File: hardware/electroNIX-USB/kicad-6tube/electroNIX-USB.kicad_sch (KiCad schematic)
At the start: 4 parts

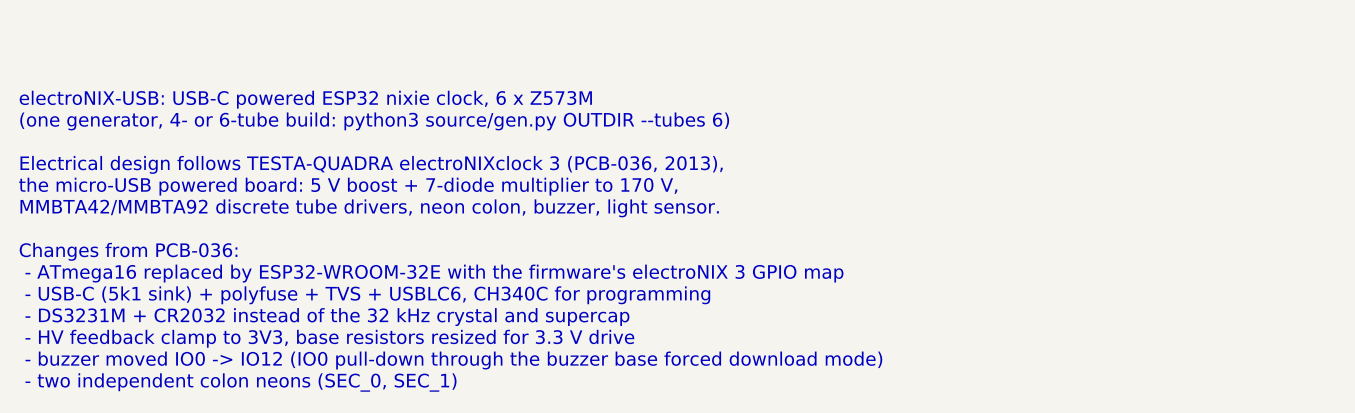
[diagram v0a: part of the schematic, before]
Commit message: electroNIX-USB: drop buzzer and DS3231, run stock firmware
Both builds now match a stock firmware profile with no changes:
BOARD_ELECTRONIX_3 for 4 tubes, BOARD_ELECTRONIX_4_6T for 6 tubes. Time
comes from NTP. IO0 gets a plain 10k pull-up. On the 4-tube build IO12
and IO15 are left open and reserved for anodes 5/6.

Co-Authored-By: Claude Opus 5.5 <noreply@anthropic.com>
Claude-Session: https://claude.ai/code/session_01AFMfevKEKDGbci8uJGhf4W
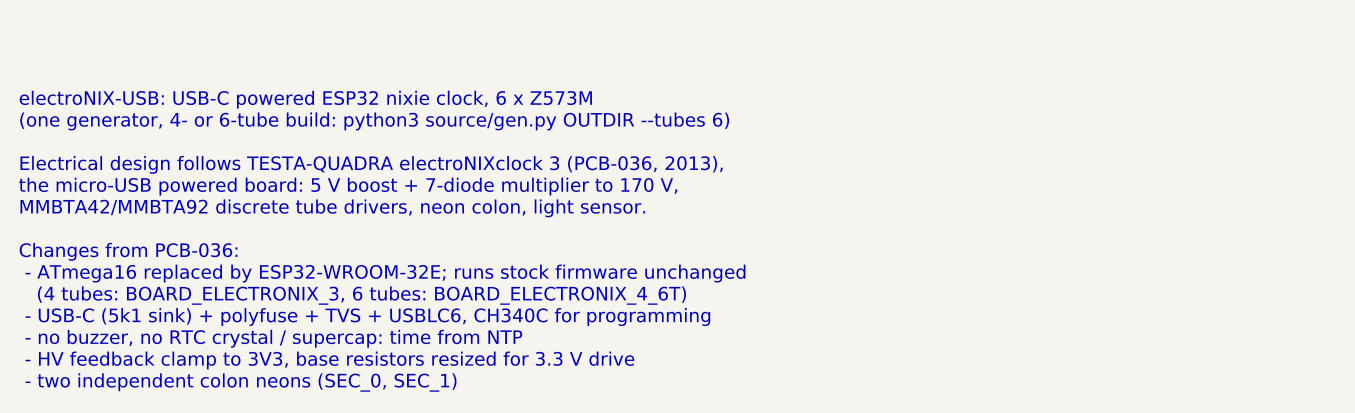
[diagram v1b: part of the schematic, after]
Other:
- note added: "electroNIX-USB: USB-C powered ESP32 nixie clock, 6 x Z573M (one generator, 4- or 6-tube build: python3 source/gen.py OUTDIR --tubes 6) Electrical design follows TESTA-QUADRA electroNIXclock 3 (PCB-036, 2013), the micro-USB powered board: 5 V boost + 7-diode multiplier to 170 V, MMBTA42/MMBTA92 discrete tube drivers, neon colon, light sensor. Changes from PCB-036: - ATmega16 replaced by ESP32-WROO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"
- note removed: "electroNIX-USB: USB-C powered ESP32 nixie clock, 6 x Z573M (one generator, 4- or 6-tube build: python3 source/gen.py OUTDIR --tubes 6) Electrical design follows TESTA-QUADRA electroNIXclock 3 (PCB-036, 2013), the micro-USB powered board: 5 V boost + 7-diode multiplier to 170 V, MMBTA42/MMBTA92 discrete tube drivers, neon colon, buzzer, light sensor. Changes from PCB-036: - ATmega16 replaced by ES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"
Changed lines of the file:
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@@
     (comment 1 "ESP32 rework of TESTA-QUADRA electroNIXclock 3 (PCB-036), USB powered")
     (comment 2 "Licensed with the repository; see LICENSE"))
-  (text "electroNIX-USB: USB-C powered ESP32 nixie clock, 6 x Z573M\n(one generator, 4- or 6-tube build: python3 source/gen.py OUTDIR --tubes 6)\n\nElectrical design follows TESTA-QUADRA electroNIXclock 3 (PCB-036, 2013),\nthe micro-USB powered board: 5 V boost + 7-diode multiplier to 170 V,\nMMBTA42/MMBTA92 discrete tube drivers, neon colon, buzzer, light sensor.\n\nChanges from PCB-036:\n - ATmega16 replaced by ESP32-WROOM-32E with the firmware's electroNIX 3 GPIO map\n - USB-C (5k1 sink) + polyfuse + TVS + USBLC6, CH340C for programming\n - DS3231M + CR2032 instead of the 32 kHz crystal and supercap\n - HV feedback clamp to 3V3, base resistors resized for 3.3 V drive\n - buzzer moved IO0 -> IO12 (IO0 pull-down through the buzzer base forced download mode)\n - two independent colon neons (SEC_0, SEC_1)"
+  (text "electroNIX-USB: USB-C powered ESP32 nixie clock, 6 x Z573M\n(one generator, 4- or 6-tube build: python3 source/gen.py OUTDIR --tubes 6)\n\nElectrical design follows TESTA-QUADRA electroNIXclock 3 (PCB-036, 2013),\nthe micro-USB powered board: 5 V boost + 7-diode multiplier to 170 V,\nMMBTA42/MMBTA92 discrete tube drivers, neon colon, light sensor.\n\nChanges from PCB-036:\n - ATmega16 replaced by ESP32-WROOM-32E; runs stock firmware unchanged\n   (4 tubes: BOARD_ELECTRONIX_3, 6 tubes: BOARD_ELECTRONIX_4_6T)\n - USB-C (5k1 sink) + polyfuse + TVS + USBLC6, CH340C for programming\n - no buzzer, no RTC crystal / supercap: time from NTP\n - HV feedback clamp to 3V3, base resistors resized for 3.3 V drive\n - two independent colon neons (SEC_0, SEC_1)"
     (at 30 180 0)
     (effects
